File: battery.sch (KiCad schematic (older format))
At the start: 41 parts, among them P1 MEGAFIT, U5 INA139

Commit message: Continued syncing with original design.
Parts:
- removed C? (x2): 0.1uF, SM0805, symbol C
- added C10, C11: 0.1uF, SM0805, symbol C
- C1, C2: renamed from C?; value 33uF -> C
- C5, C9: Digikey (none) -> 399-11163-1-ND
- C6: Digikey (none) -> 478-3769-1-ND
- C7, C8: renamed from C?; Digikey (none) -> 478-3769-1-ND
- D1, D2: renamed from D?; value LED -> LED Green; Digikey (none) -> L62415CT-ND
- J1: renamed from P1; value MEGAFIT -> MEGAFIT-4SKT; Digikey (none) -> WM10392-ND
- R10: renamed from R?; value R -> 75k; Digikey (none) -> P75KDACT-ND
- R11: renamed from R?; value LVK25 -> 10mOhm; Digikey (none) -> LVK25R010DERCT-ND
- R12: renamed from R?; value R -> 47.5k; Digikey (none) -> P47.5KDACT-ND
- R13: renamed from R?; value R -> 150; Digikey (none) -> P150DACT-ND
- R5: value LVK25R002DER -> 2mOhm 0.5%; Digikey (none) -> LVK25R002DERCT-ND
- R6: Digikey (none) -> P68.1KDACT-ND
- R7: Digikey (none) -> P10KBFCT-ND
- R8: Digikey (none) -> P1.3KBFCT-ND
- R9: renamed from R?; value LVK25 -> 2mOhm 0.5%; Digikey (none) -> LVK25R002DERCT-ND
- SW1: renamed from SW?; Digikey (none) -> 123
- gave numbers to parts that had none: 18
- renumbered U5 to U6
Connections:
- net +5V: now also C10.1, C11.1
- net GND: now also C10.2, C11.2

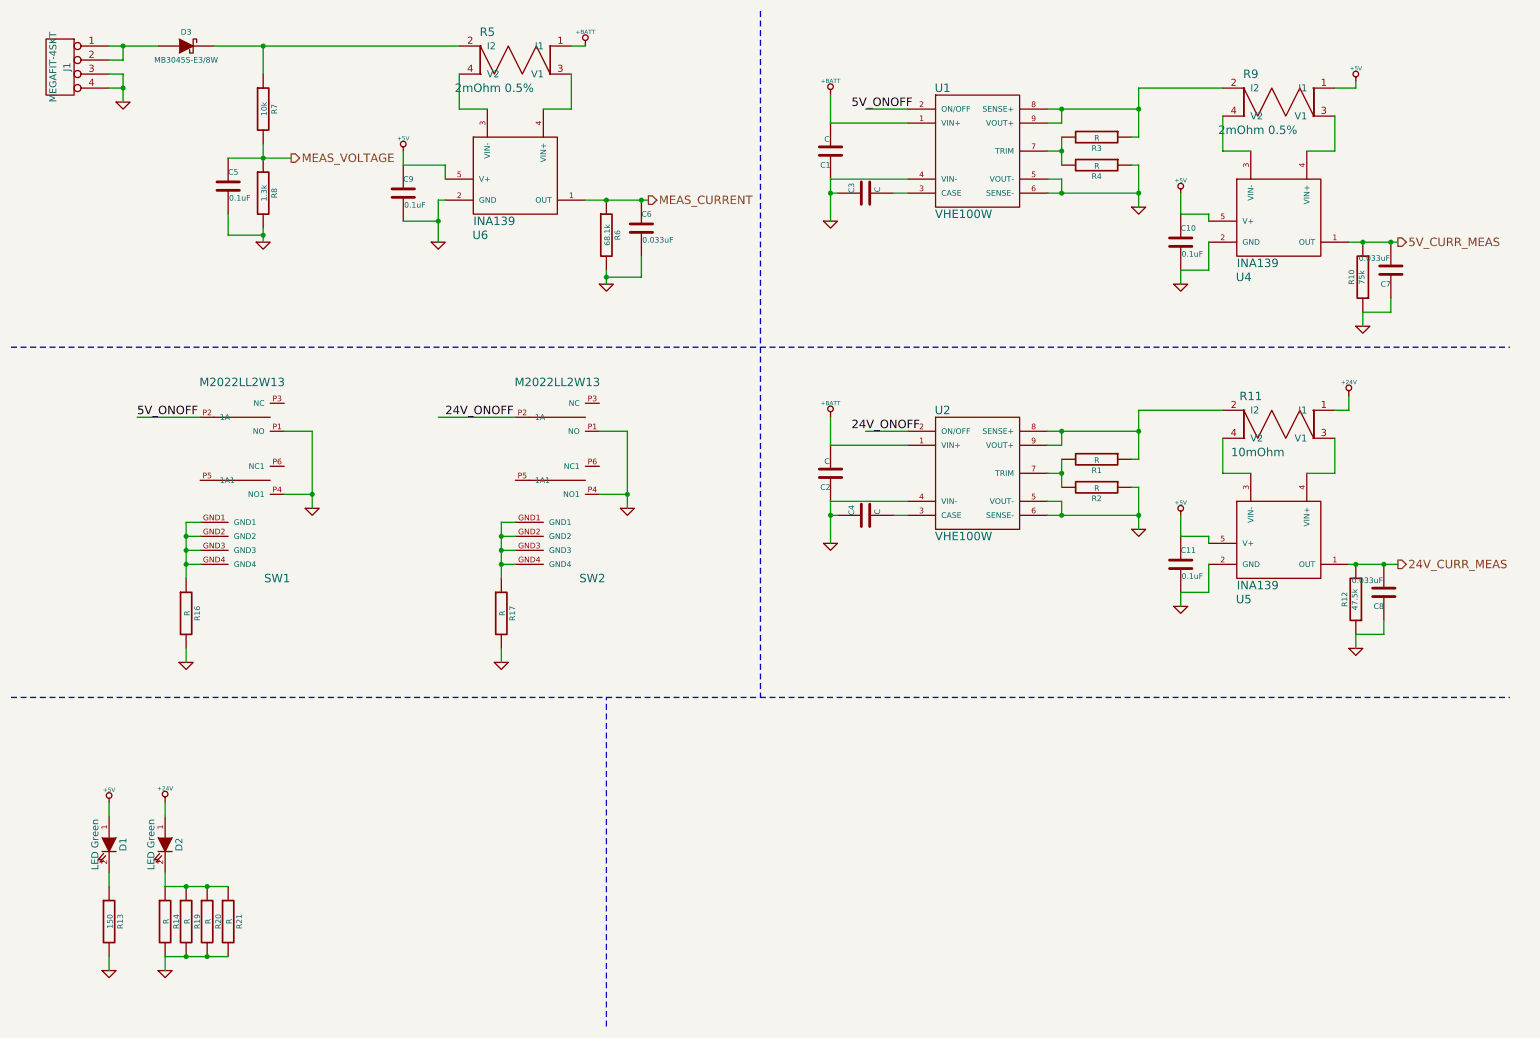
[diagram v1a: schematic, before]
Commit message: Finishing bom integration with schematic.
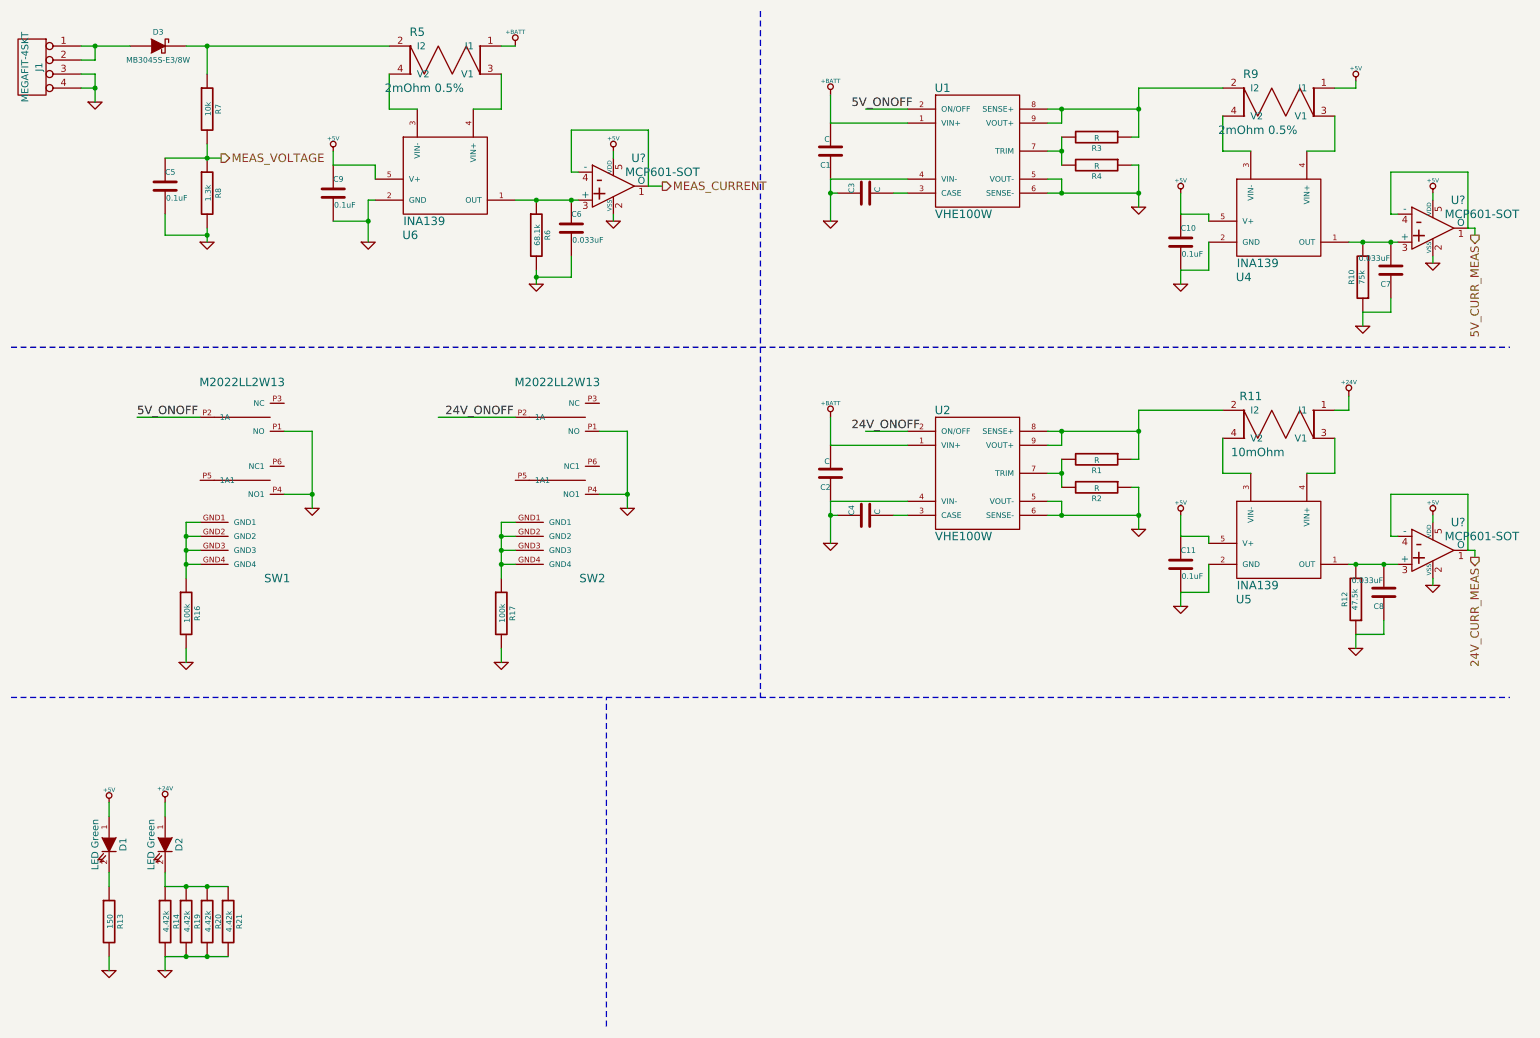
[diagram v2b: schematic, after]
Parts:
- added U? (x3): MCP601-SOT, ~, symbol MCP601-SOT
- D1, D2: Digikey L62415CT-ND -> 160-1218-1-ND
- D3: Digikey (none) -> MB3045S-E3/8WGICT-ND
- R14, R19, R20, R21: value R -> 4.42k; Digikey (none) -> P4.42KCCT-ND
- R16, R17: value R -> 100k; Digikey (none) -> P100KACT-ND
- SW1: Digikey 123 -> 360-3095-ND
- SW2: Digikey (none) -> 360-3095-ND
- U1: Digikey (none) -> 102-2639-ND
- U2: Digikey (none) -> 102-2260-ND
- U4, U5, U6: Digikey (none) -> 296-26061-1-ND
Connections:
- net +5V: now also U?.5 (VDD), U?.5 (VDD), U?.5 (VDD)
- net 24V_CURR_MEAS: now also U?.1 (O), U?.4 (-); no longer C8.2, R12.2, U5.1 (OUT)
- net 5V_CURR_MEAS: now also U?.1 (O), U?.4 (-); no longer C7.2, R10.2, U4.1 (OUT)
- net GND: now also U?.2 (VSS), U?.2 (VSS), U?.2 (VSS)
- net MEAS_CURRENT: now also U?.1 (O), U?.4 (-); no longer C6.1, R6.1, U6.1 (OUT)
- new net: C6.1, R6.1, U6.1 (OUT), U?.3 (+)
- new net: C7.2, R10.2, U4.1 (OUT), U?.3 (+)
- new net: C8.2, R12.2, U5.1 (OUT), U?.3 (+)
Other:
- moved on the sheet: C5, C6, C9, D3, J1, R5, R6, R7, R8, U6

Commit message: Adding buffer on voltage reference output.
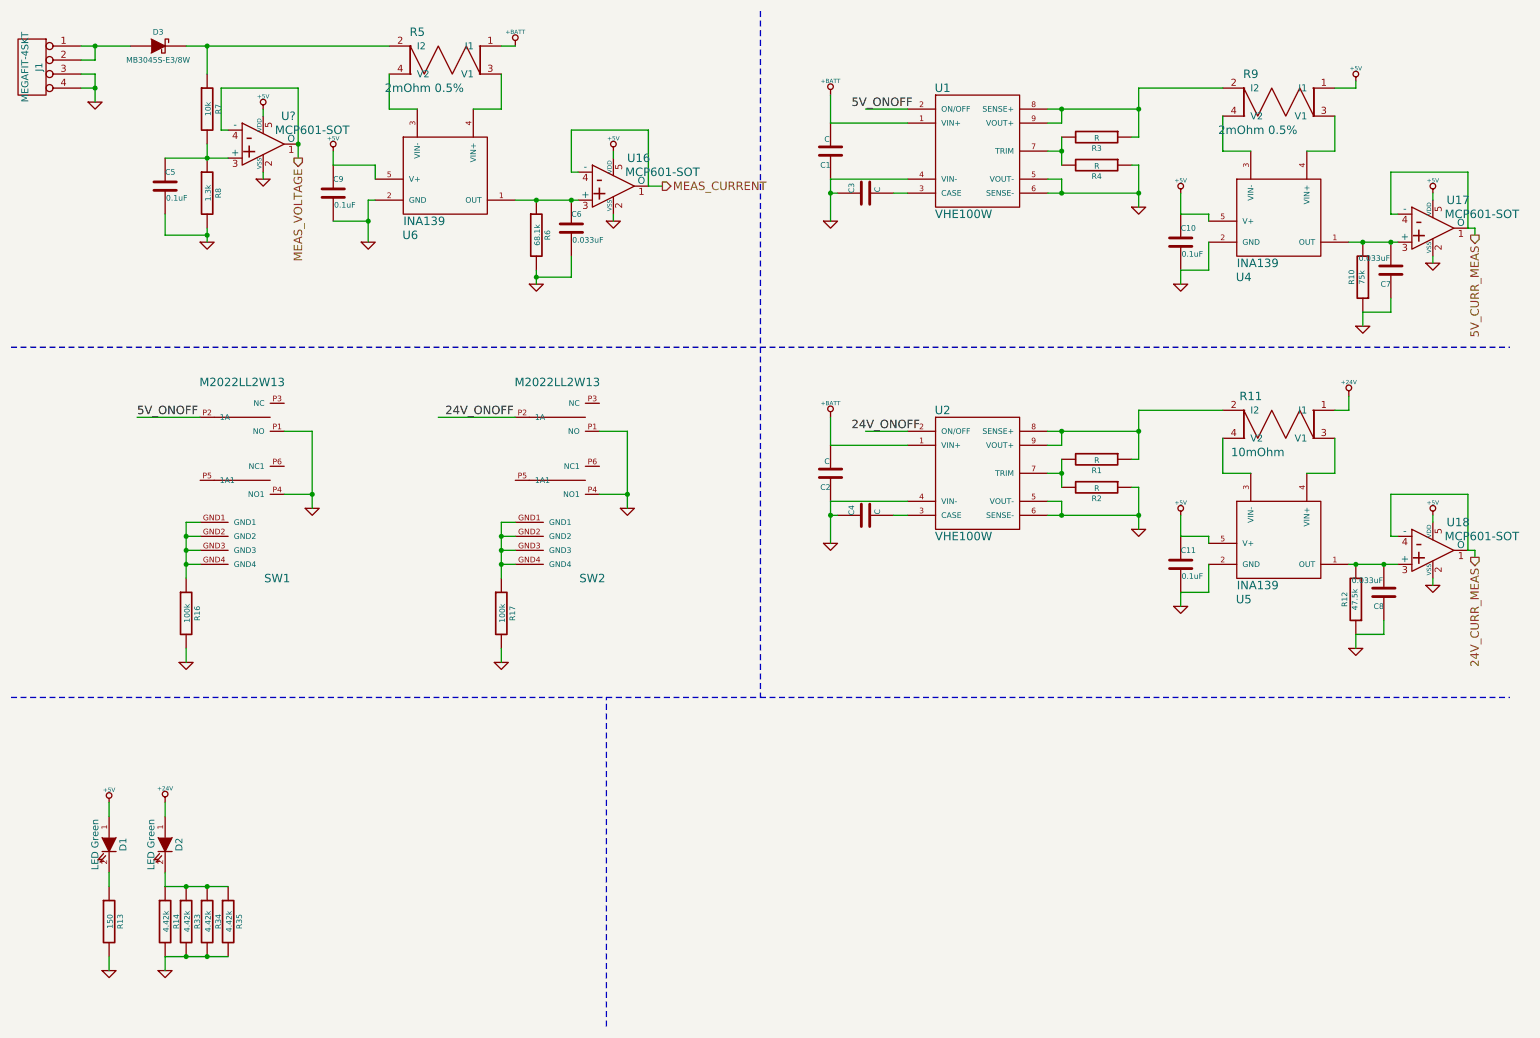
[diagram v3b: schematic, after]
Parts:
- added U?: MCP601-SOT, ~, symbol MCP601-SOT
- gave numbers to parts that had none: 3
- renumbered R19 to R33, R20 to R34, R21 to R35
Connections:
- net +5V: now also U?.5 (VDD)
- net GND: now also U?.2 (VSS)
- net MEAS_VOLTAGE: now also U?.1 (O), U?.4 (-); no longer C5.1, R7.2, R8.1
- new net: C5.1, R7.2, R8.1, U?.3 (+)
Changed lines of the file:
@@
 	1    0    0    -1
 $EndComp
-Text HLabel 2000 1550 2    60   Output ~ 0
+Text HLabel 2550 1550 3    60   Output ~ 0
 MEAS_VOLTAGE
 $Comp
@@
 	1900 1550 1900 1450
 Wire Wire Line
-	1600 1550 2000 1550
-Wire Wire Line
 	1900 2050 1900 2150
-Connection ~ 1900 1550
 Wire Wire Line
 	1600 1950 1600 2100
@@
 $EndComp
 $Comp
-L R R19
+L R R33
 U 1 1 55D76DE0
 P 1750 7000
-F 0 "R19" V 1830 7000 40  0000 C CNN
+F 0 "R33" V 1830 7000 40  0000 C CNN
 F 1 "4.42k" V 1757 7001 40  0000 C CNN
 F 2 "SM0805" V 1680 7000 30  0001 C CNN
@@
 $EndComp
 $Comp
-L R R20
+L R R34
 U 1 1 55D76DE7
 P 1900 7000
-F 0 "R20" V 1980 7000 40  0000 C CNN
+F 0 "R34" V 1980 7000 40  0000 C CNN
 F 1 "4.42k" V 1907 7001 40  0000 C CNN
 F 2 "SM0805" V 1830 7000 30  0001 C CNN
@@
 $EndComp
 $Comp
-L R R21
+L R R35
 U 1 1 55D76DEE
 P 2050 7000
-F 0 "R21" V 2130 7000 40  0000 C CNN
+F 0 "R35" V 2130 7000 40  0000 C CNN
 F 1 "4.42k" V 2057 7001 40  0000 C CNN
 F 2 "SM0805" V 1980 7000 30  0001 C CNN
@@
 $EndComp
 $Comp
-L MCP601-SOT U?
+L MCP601-SOT U16
 U 1 1 55D797DB
 P 4800 1750
-F 0 "U?" H 4980 1950 60  0000 C CNN
+F 0 "U16" H 4980 1950 60  0000 C CNN
 F 1 "MCP601-SOT" H 5150 1850 60  0000 C CNN
 F 2 "~" H 4800 1750 60  0000 C CNN
@@
 $EndComp
 $Comp
-L +5V #PWR?
+L +5V #PWR029
 U 1 1 55D79834
 P 4800 1500
-F 0 "#PWR?" H 4800 1590 20  0001 C CNN
+F 0 "#PWR029" H 4800 1590 20  0001 C CNN
 F 1 "+5V" H 4800 1590 30  0000 C CNN
 F 2 "" H 4800 1500 60  0000 C CNN
@@
 	4800 1550 4800 1500
 $Comp
-L GND #PWR?
+L GND #PWR030
 U 1 1 55D79909
 P 4800 2000
-F 0 "#PWR?" H 4800 2000 30  0001 C CNN
+F 0 "#PWR030" H 4800 2000 30  0001 C CNN
 F 1 "GND" H 4800 1930 30  0001 C CNN
 F 2 "" H 4800 2000 60  0000 C CNN
@@
 	5050 1750 5150 1750
 $Comp
-L MCP601-SOT U?
+L MCP601-SOT U17
 U 1 1 55D79F1C
 P 10650 2050
-F 0 "U?" H 10830 2250 60  0000 C CNN
+F 0 "U17" H 10830 2250 60  0000 C CNN
 F 1 "MCP601-SOT" H 11000 2150 60  0000 C CNN
 F 2 "~" H 10650 2050 60  0000 C CNN
@@
 $EndComp
 $Comp
-L MCP601-SOT U?
+L MCP601-SOT U18
 U 1 1 55D79F2F
 P 10650 4350
-F 0 "U?" H 10830 4550 60  0000 C CNN
+F 0 "U18" H 10830 4550 60  0000 C CNN
 F 1 "MCP601-SOT" H 11000 4450 60  0000 C CNN
 F 2 "~" H 10650 4350 60  0000 C CNN
@@
 	10950 2050 10900 2050
 $Comp
-L GND #PWR?
+L GND #PWR031
 U 1 1 55D7A034
 P 10650 2300
-F 0 "#PWR?" H 10650 2300 30  0001 C CNN
+F 0 "#PWR031" H 10650 2300 30  0001 C CNN
 F 1 "GND" H 10650 2230 30  0001 C CNN
 F 2 "" H 10650 2300 60  0000 C CNN
@@
 $EndComp
 $Comp
-L +5V #PWR?
+L +5V #PWR032
 U 1 1 55D7A03A
 P 10650 1800
-F 0 "#PWR?" H 10650 1890 20  0001 C CNN
+F 0 "#PWR032" H 10650 1890 20  0001 C CNN
 F 1 "+5V" H 10650 1890 30  0000 C CNN
 F 2 "" H 10650 1800 60  0000 C CNN
@@
 	10350 1950 10400 1950
 $Comp
-L GND #PWR?
+L GND #PWR033
 U 1 1 55D7A291
 P 10650 4600
-F 0 "#PWR?" H 10650 4600 30  0001 C CNN
+F 0 "#PWR033" H 10650 4600 30  0001 C CNN
 F 1 "GND" H 10650 4530 30  0001 C CNN
 F 2 "" H 10650 4600 60  0000 C CNN
@@
 $EndComp
 $Comp
-L +5V #PWR?
+L +5V #PWR034
 U 1 1 55D7A297
 P 10650 4100
-F 0 "#PWR?" H 10650 4190 20  0001 C CNN
+F 0 "#PWR034" H 10650 4190 20  0001 C CNN
 F 1 "+5V" H 10650 4190 30  0000 C CNN
 F 2 "" H 10650 4100 60  0000 C CNN
@@
 Wire Wire Line
 	10950 4350 10950 4400
+$Comp
+L MCP601-SOT U?
+U 1 1 55D846AD
+P 2300 1450
+F 0 "U?" H 2480 1650 60  0000 C CNN
+F 1 "MCP601-SOT" H 2650 1550 60  0000 C CNN
+F 2 "~" H 2300 1450 60  0000 C CNN
+F 3 "~" H 2300 1450 60  0000 C CNN
+F 4 "MCP601T-I/OTCT-ND" H 2300 1450 60  0001 C CNN "Digikey"
+	1    2300 1450
+	1    0    0    -1
+$EndComp
+$Comp
+L +5V #PWR?
+U 1 1 55D846C2
+P 2300 1200
+F 0 "#PWR?" H 2300 1290 20  0001 C CNN
+F 1 "+5V" H 2300 1290 30  0000 C CNN
+F 2 "" H 2300 1200 60  0000 C CNN
+F 3 "" H 2300 1200 60  0000 C CNN
+	1    2300 1200
+	1    0    0    -1
+$EndComp
+$Comp
+L GND #PWR?
+U 1 1 55D846C8
+P 2300 1700
+F 0 "#PWR?" H 2300 1700 30  0001 C CNN
+F 1 "GND" H 2300 1630 30  0001 C CNN
+F 2 "" H 2300 1700 60  0000 C CNN
+F 3 "" H 2300 1700 60  0000 C CNN
+	1    2300 1700
+	1    0    0    -1
+$EndComp
+Wire Wire Line
+	2300 1700 2300 1650
+Wire Wire Line
+	2300 1250 2300 1200
+Wire Wire Line
+	2550 1050 2550 1550
+Wire Wire Line
+	2550 1050 2000 1050
+Wire Wire Line
+	2000 1050 2000 1350
+Wire Wire Line
+	2000 1350 2050 1350
+Wire Wire Line
+	1600 1550 2050 1550
+Connection ~ 1900 1550
+Connection ~ 2550 1450
 $EndSCHEMATC

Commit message: Fixing number on new buffer.
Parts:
- gave numbers to parts that had none: 1
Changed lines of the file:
@@
 	10950 4350 10950 4400
 $Comp
-L MCP601-SOT U?
+L MCP601-SOT U19
 U 1 1 55D846AD
 P 2300 1450
-F 0 "U?" H 2480 1650 60  0000 C CNN
+F 0 "U19" H 2480 1650 60  0000 C CNN
 F 1 "MCP601-SOT" H 2650 1550 60  0000 C CNN
 F 2 "~" H 2300 1450 60  0000 C CNN
@@
 $EndComp
 $Comp
-L +5V #PWR?
+L +5V #PWR035
 U 1 1 55D846C2
 P 2300 1200
-F 0 "#PWR?" H 2300 1290 20  0001 C CNN
+F 0 "#PWR035" H 2300 1290 20  0001 C CNN
 F 1 "+5V" H 2300 1290 30  0000 C CNN
 F 2 "" H 2300 1200 60  0000 C CNN
@@
 $EndComp
 $Comp
-L GND #PWR?
+L GND #PWR036
 U 1 1 55D846C8
 P 2300 1700
-F 0 "#PWR?" H 2300 1700 30  0001 C CNN
+F 0 "#PWR036" H 2300 1700 30  0001 C CNN
 F 1 "GND" H 2300 1630 30  0001 C CNN
 F 2 "" H 2300 1700 60  0000 C CNN
